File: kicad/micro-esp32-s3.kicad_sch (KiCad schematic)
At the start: 69 parts, among them IC1 IRM-H638T/TR2, J1 TYPE-C-31-M-12, J3 DM3D-SF, Q1 NTA4151PT1G, Q2 NTA4151PT1G, Q3 NTA4151PT1G, U1 NCP167BMX330TBG, U2 ESP32-S3-WROOM-1, U3 MAX98357AETE+T, U4 TP4057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

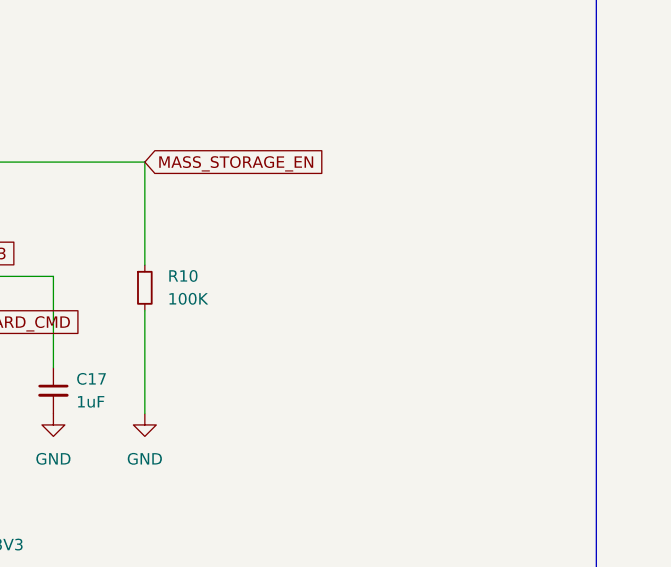
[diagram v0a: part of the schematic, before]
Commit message: Change pull down resistor on mass storage enable to 1K
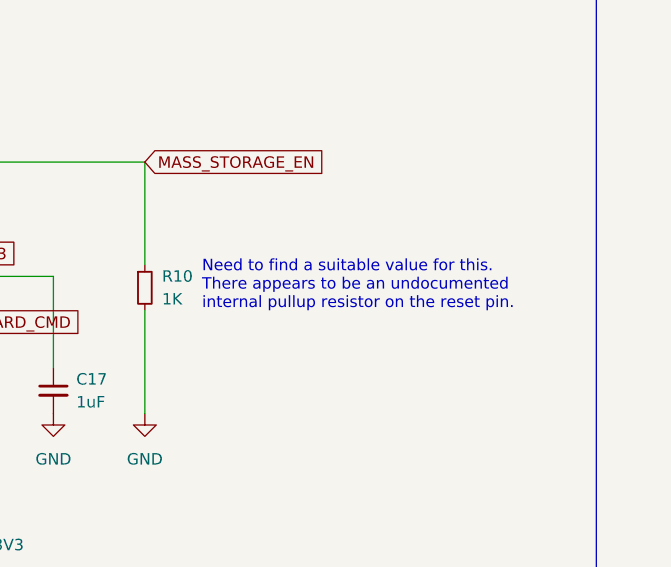
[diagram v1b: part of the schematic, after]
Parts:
- R10: value 100K -> 1K
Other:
- note added: "Need to find a suitable value for this. There appears to be an undocumented internal pullup resistor on the reset pin."
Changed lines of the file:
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@@
     (effects (font (size 1.27 1.27)) (justify left top))
   )
+  (text "Need to find a suitable value for this.\nThere appears to be an undocumented\ninternal pullup resistor on the reset pin."
+    (at 354.965 59.055 0)
+    (effects (font (size 1.27 1.27)) (justify left bottom))
+  )
   (global_label "SPK_BCLK" (shape input) (at 162.56 142.875 0) (fields_autoplaced)
     (effects (font (size 1.27 1.27)) (justify left))
@@
   (symbol (lib_id "Device:R_Small") (at 348.615 56.515 0) (unit 1)
     (in_bom yes) (on_board yes) (dnp no) (fields_autoplaced)
-    (property "Reference" "R10" (at 351.155 55.245 0)
+    (property "Reference" "R10" (at 350.52 55.245 0)
       (effects (font (size 1.27 1.27)) (justify left))
     )
-    (property "Value" "100K" (at 351.155 57.785 0)
+    (property "Value" "1K" (at 350.52 57.785 0)
       (effects (font (size 1.27 1.27)) (justify left))
     )

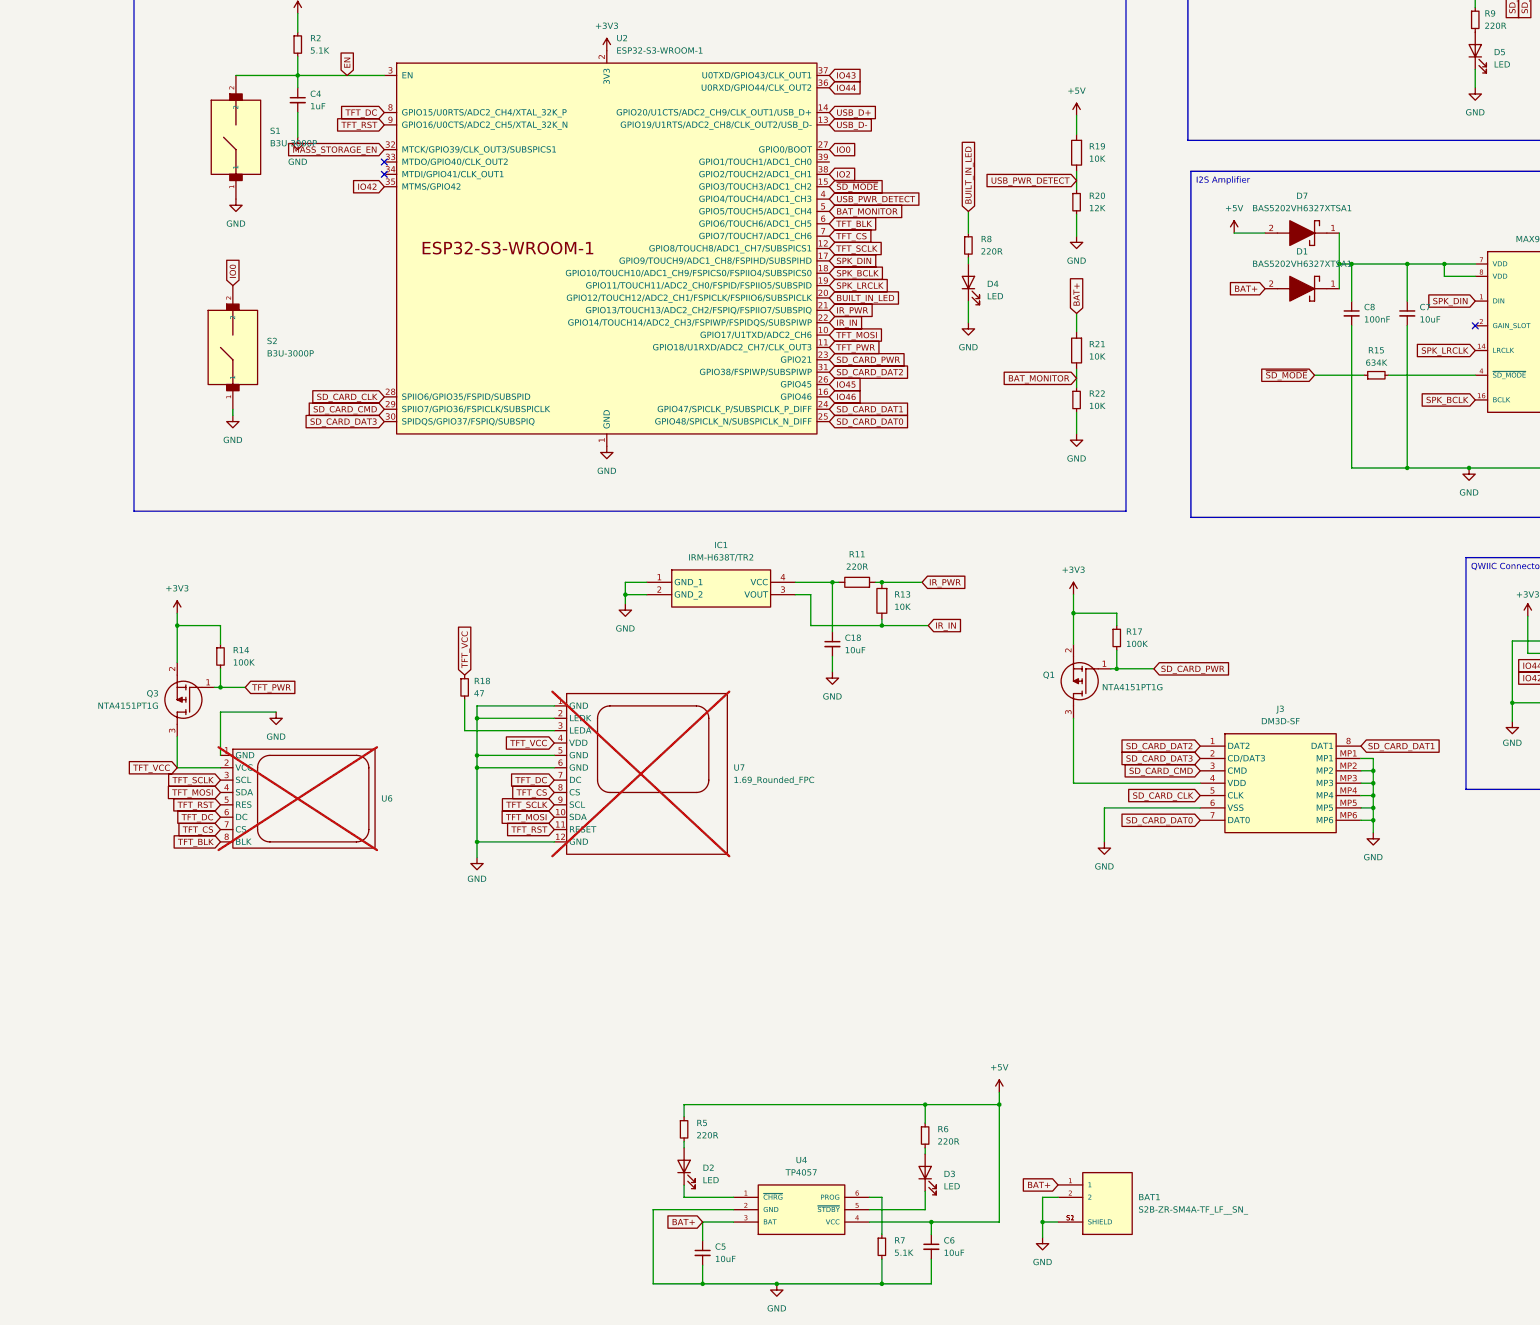
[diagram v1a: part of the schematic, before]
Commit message: Clean up schematic
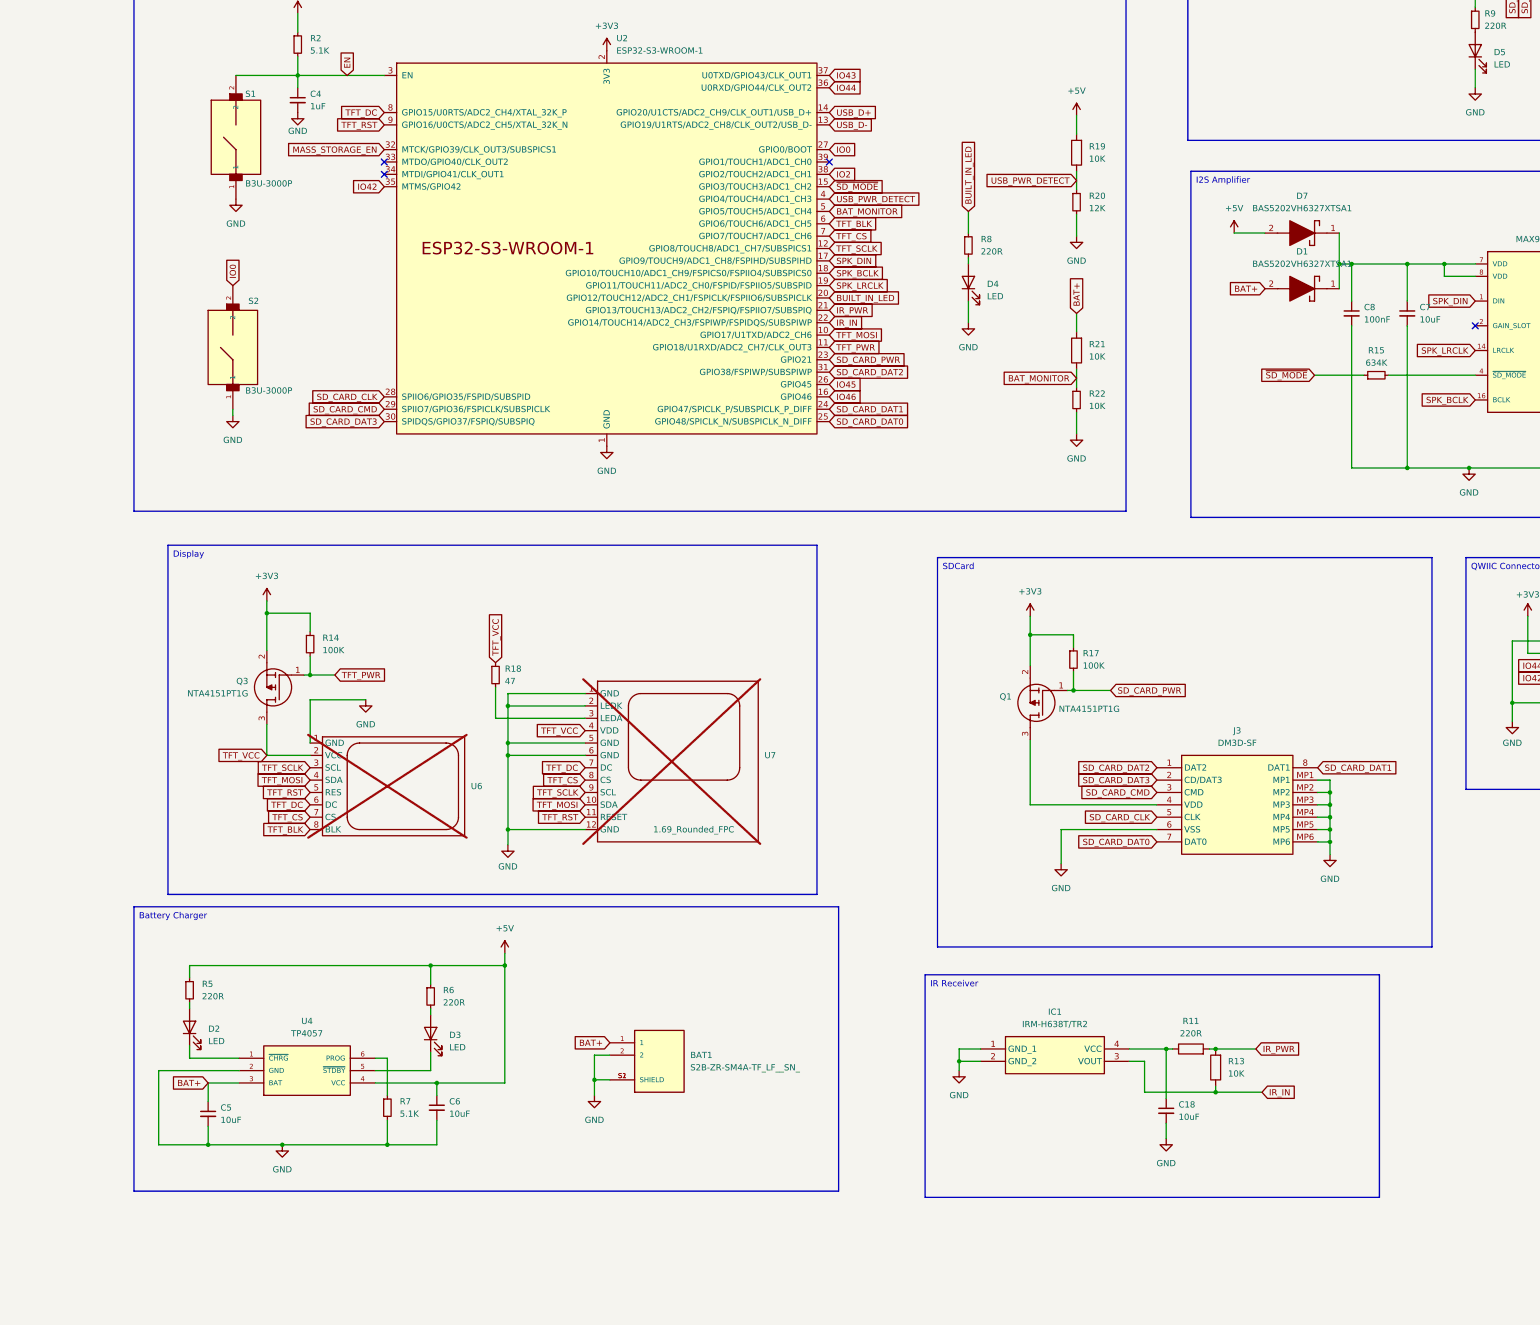
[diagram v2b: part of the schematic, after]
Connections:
- no-connect marks 13 -> 14
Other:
- moved on the sheet: BAT1, C18, C5, C6, D2, D3, IC1, J3, Q1, Q3, R11, R13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

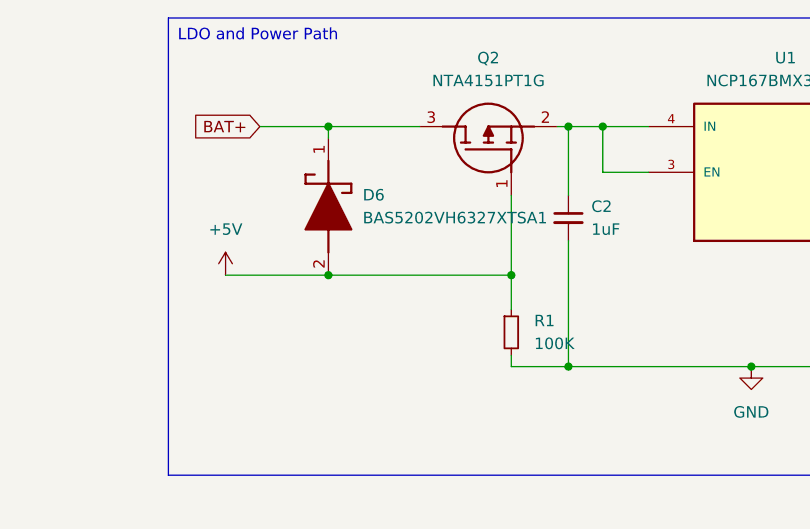
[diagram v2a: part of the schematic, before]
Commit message: Fix power path in schematic
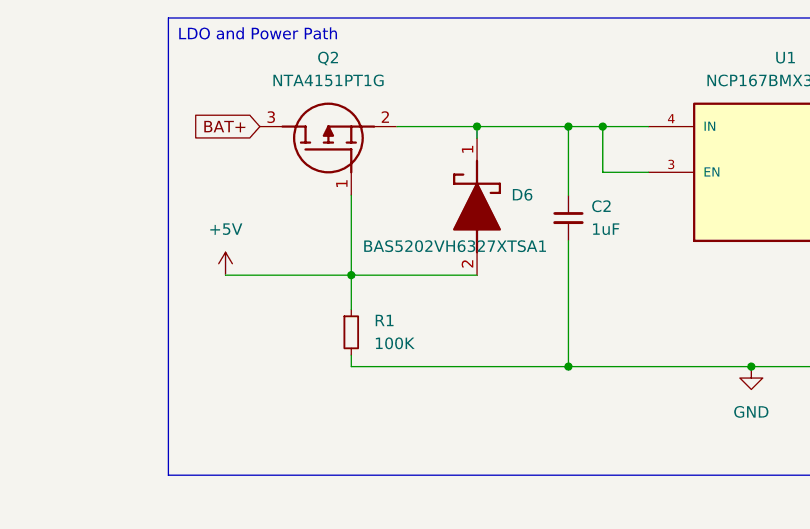
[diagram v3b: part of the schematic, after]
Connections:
- net BAT+: no longer D6.1 (K)
- net at C2.1, Q2.2 (S), U1.3 (EN)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: now also D6.1 (K)
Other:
- moved on the sheet: Q2, R1

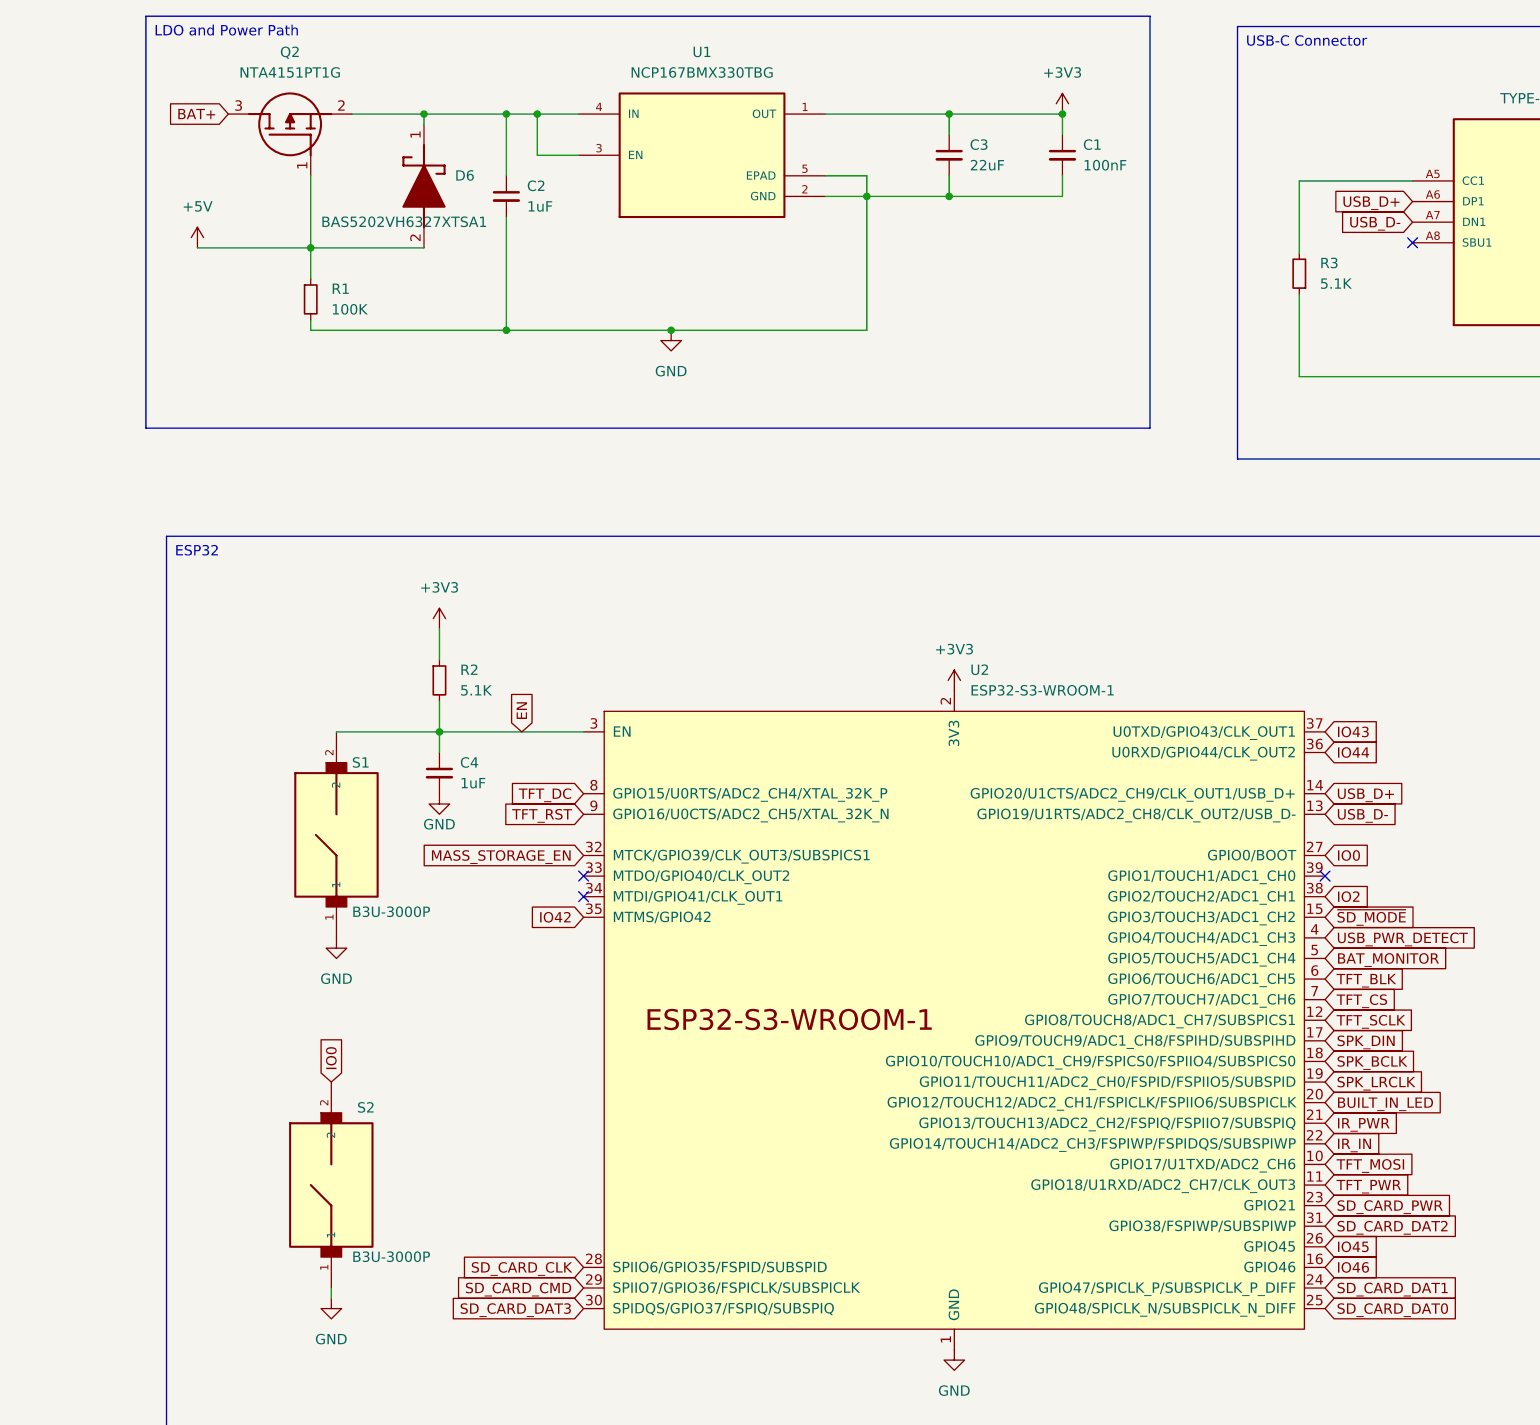
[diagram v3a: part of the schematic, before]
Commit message: Make sure GPIO45 and GPIO46 are disconnected
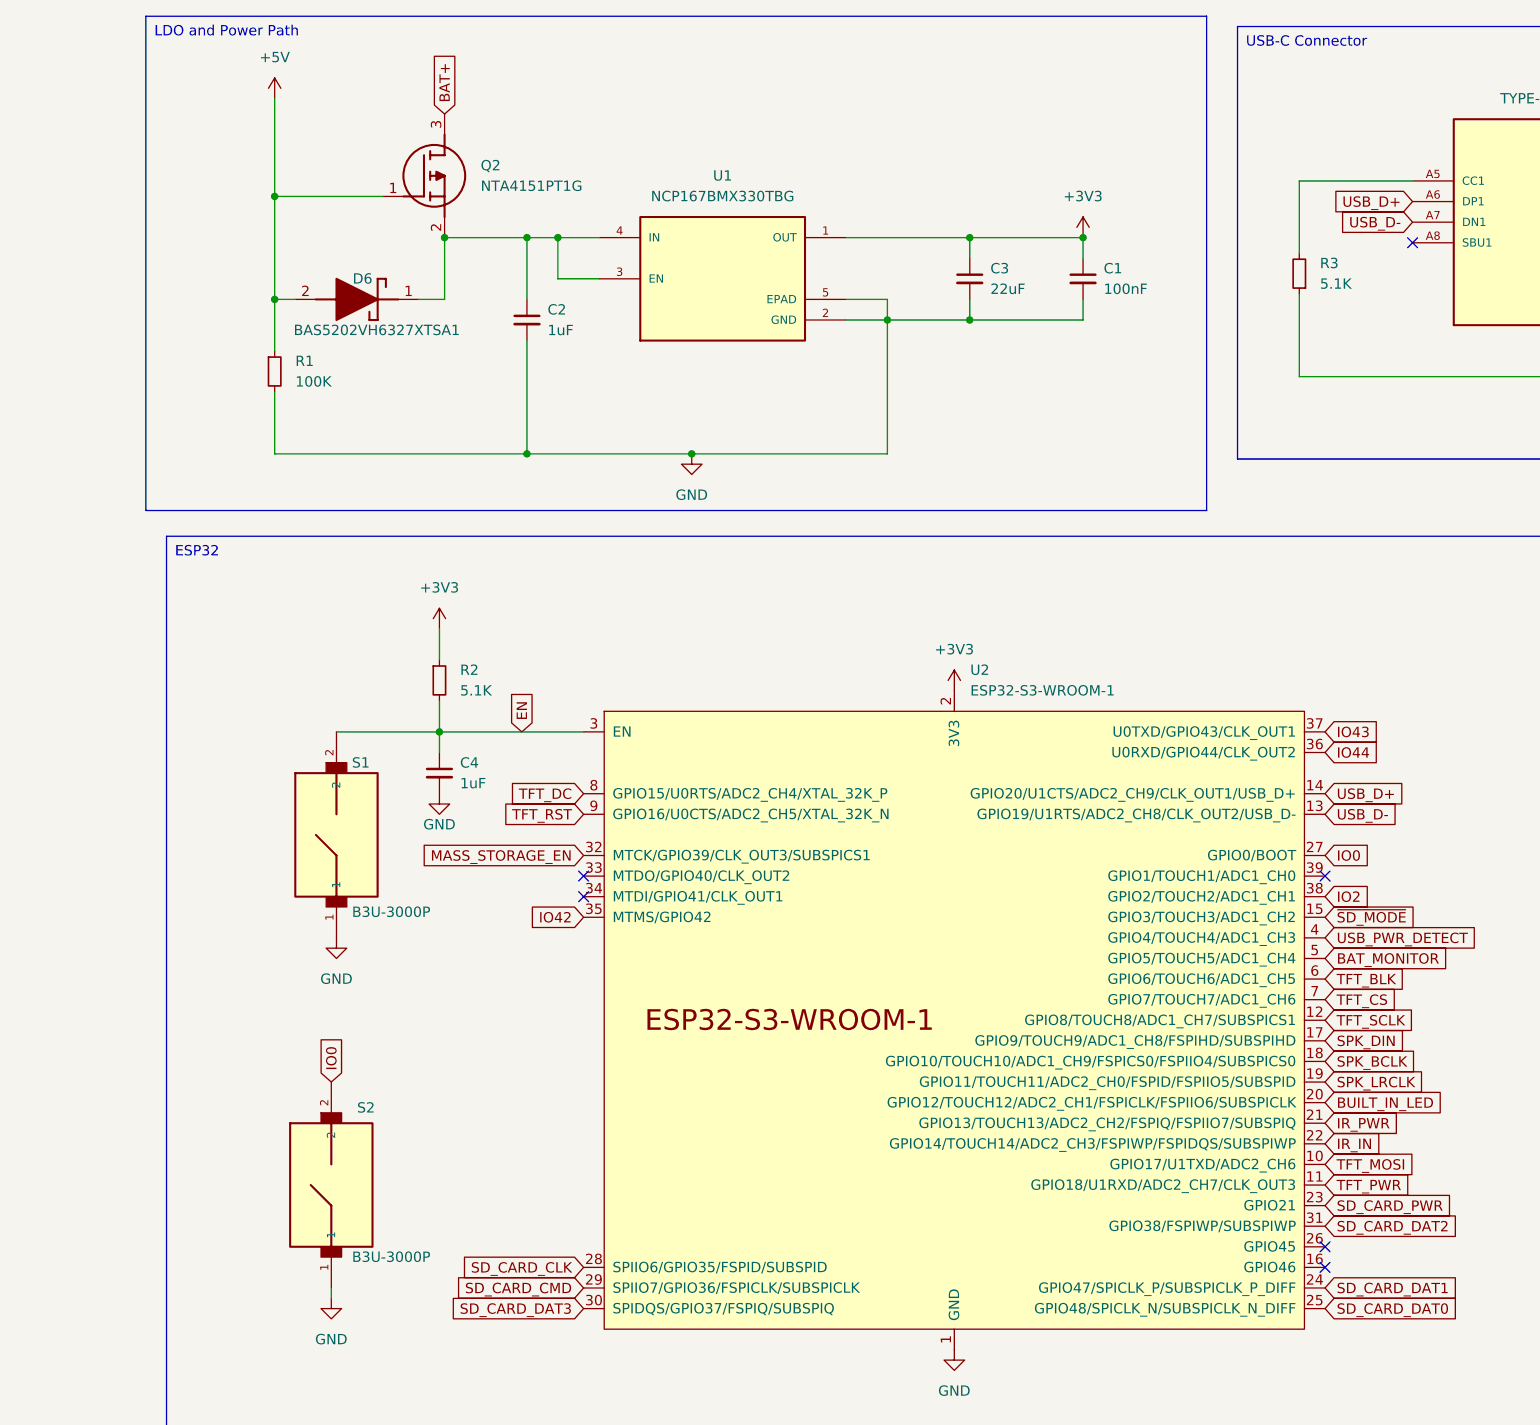
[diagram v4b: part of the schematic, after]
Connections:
- net IO45: no longer names the net of U2.26 (GPIO45)
- net IO46: no longer names the net of U2.16 (GPIO46)
- no-connect marks 14 -> 16
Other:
- moved on the sheet: C1, C2, C3, D6, Q2, R1, U1
